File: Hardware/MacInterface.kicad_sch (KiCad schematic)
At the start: 11 parts, among them J1 650946-5, U2 SN74LVCH16T245, U3 SN74LVCH16T245, U4 SN74LVCH16T245, U5 68000-CPU, U6 68000-BOARD

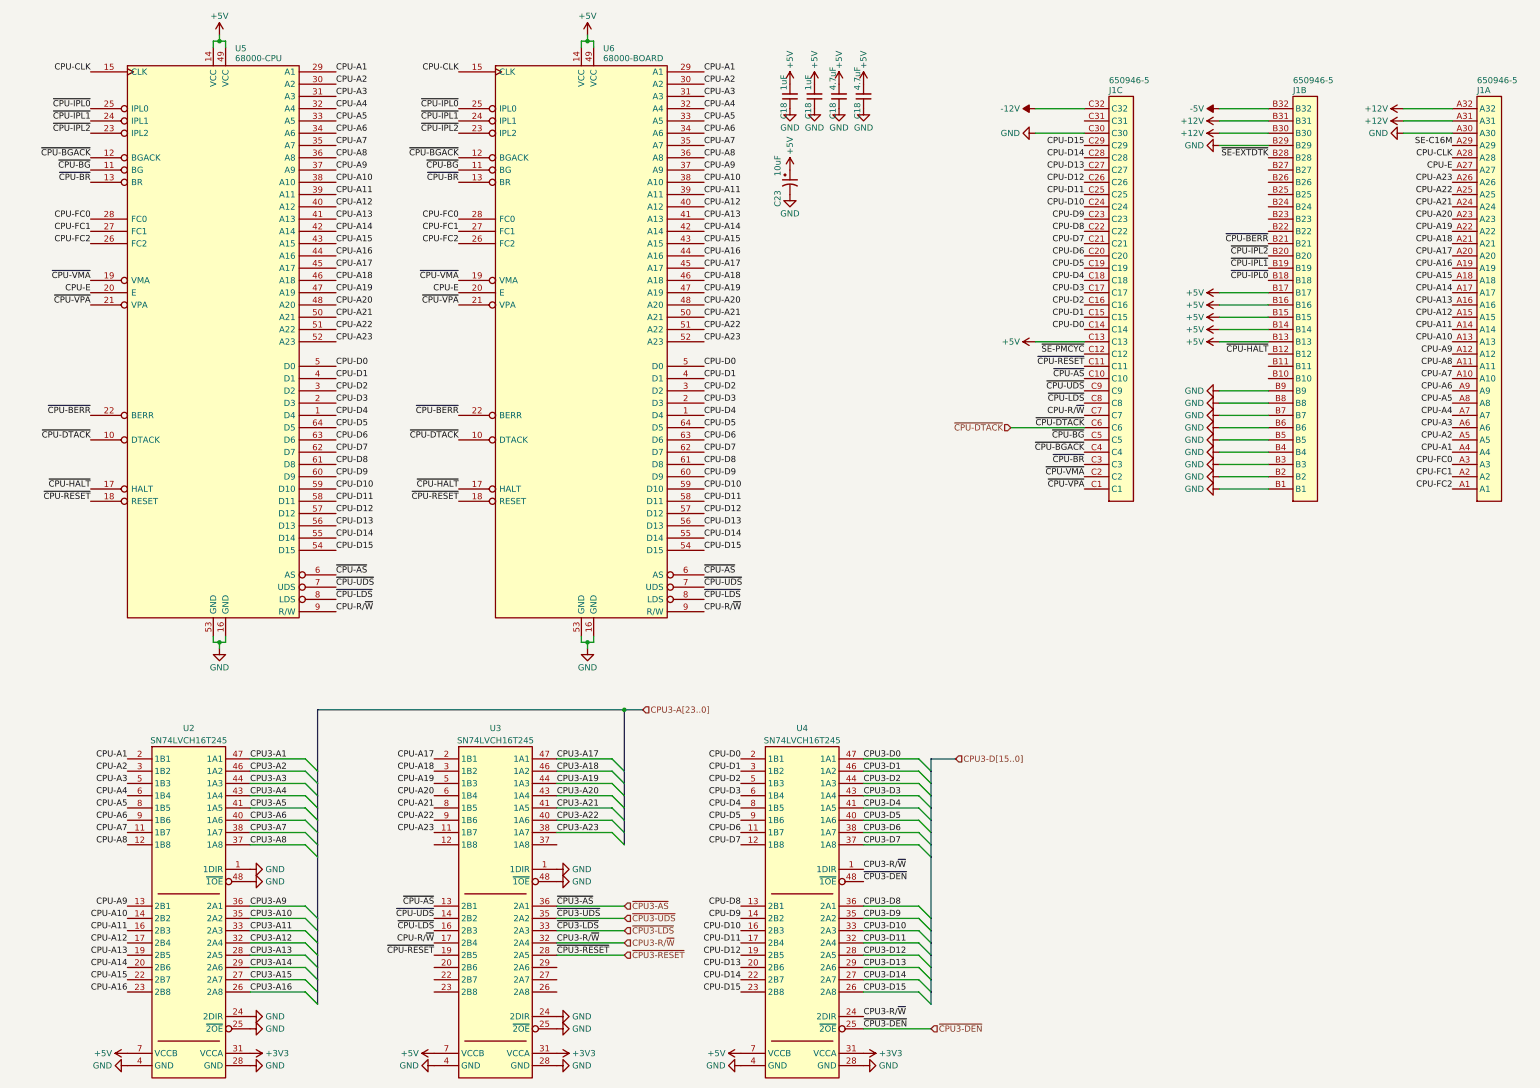
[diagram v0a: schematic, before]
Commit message: R3 Initial schematic complete, start routing
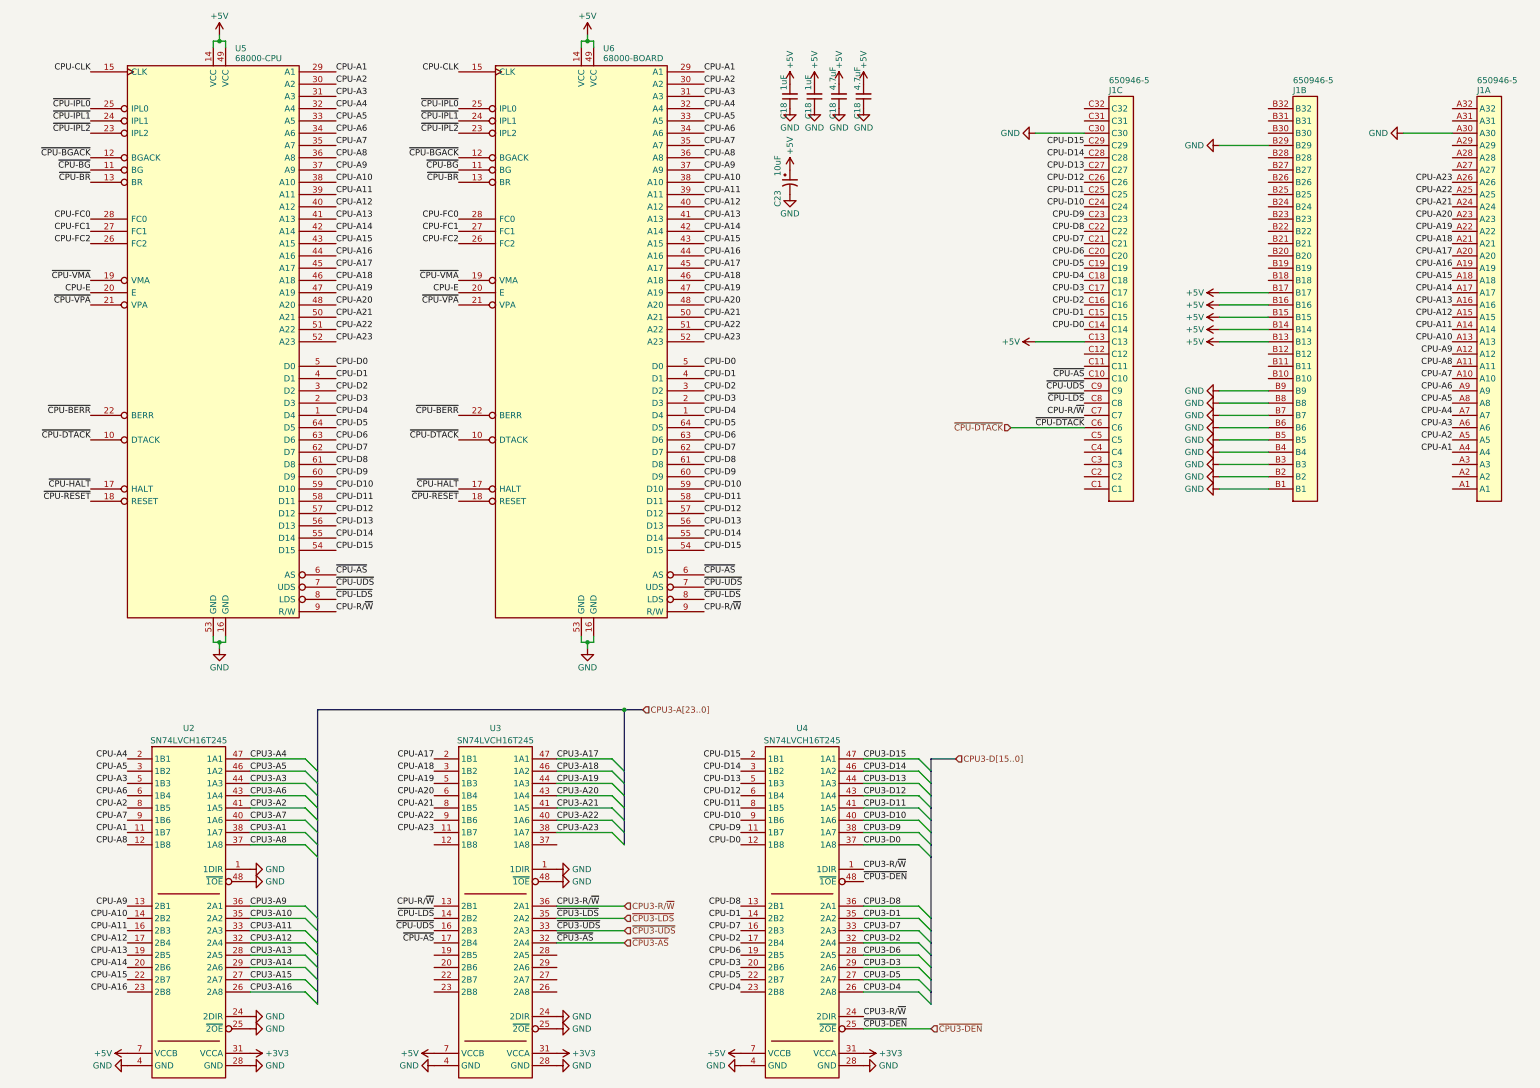
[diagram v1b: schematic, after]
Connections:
- net ~{CPU3-RESET} is gone; now on net GND: U3.28 (GND)
- net CPU-A1: now also U2.11 (1B7); no longer U2.2 (1B1)
- net CPU-A2: now also U2.8 (1B5); no longer U2.3 (1B2)
- net CPU-A4: now also U2.2 (1B1); no longer U2.6 (1B4)
- net CPU-A5: now also U2.3 (1B2); no longer U2.8 (1B5)
- net CPU-A6: now also U2.6 (1B4); no longer U2.9 (1B6)
- net CPU-A7: now also U2.9 (1B6); no longer U2.11 (1B7)
- net CPU-CLK: no longer J1.A28
- net CPU-D0: now also U4.12 (1B8); no longer U4.2 (1B1)
- net CPU-D1: now also U4.14 (2B2); no longer U4.3 (1B2)
- net CPU-D10: now also U4.9 (1B6); no longer U4.16 (2B3)
- net CPU-D11: now also U4.8 (1B5); no longer U4.17 (2B4)
- net CPU-D12: now also U4.6 (1B4); no longer U4.19 (2B5)
- net CPU-D13: now also U4.5 (1B3); no longer U4.20 (2B6)
- net CPU-D14: now also U4.3 (1B2); no longer U4.22 (2B7)
- net CPU-D15: now also U4.2 (1B1); no longer U4.23 (2B8)
- net CPU-D2: now also U4.17 (2B4); no longer U4.5 (1B3)
- net CPU-D3: now also U4.20 (2B6); no longer U4.6 (1B4)
- net CPU-D4: now also U4.23 (2B8); no longer U4.8 (1B5)
- net CPU-D5: now also U4.22 (2B7); no longer U4.9 (1B6)
- net CPU-D6: now also U4.19 (2B5); no longer U4.11 (1B7)
- net CPU-D7: now also U4.16 (2B3); no longer U4.12 (1B8)
- net CPU-D9: now also U4.11 (1B7); no longer U4.14 (2B2)
- net CPU-E: no longer J1.A27
- net CPU-FC0: no longer J1.A3
- net CPU-FC1: no longer J1.A2
- net CPU-FC2: no longer J1.A1
- net CPU-R/~{W}: now also U3.13 (2B1); no longer U3.17 (2B4)
- net CPU3-A1: now also U2.38 (1A7); no longer U2.47 (1A1)
- net CPU3-A2: now also U2.41 (1A5); no longer U2.46 (1A2)
- net CPU3-A4: now also U2.47 (1A1); no longer U2.43 (1A4)
- net CPU3-A5: now also U2.46 (1A2); no longer U2.41 (1A5)
- net CPU3-A6: now also U2.43 (1A4); no longer U2.40 (1A6)
- net CPU3-A7: now also U2.40 (1A6); no longer U2.38 (1A7)
- net CPU3-D0: now also U4.37 (1A8); no longer U4.47 (1A1)
- net CPU3-D1: now also U4.35 (2A2); no longer U4.46 (1A2)
- net CPU3-D10: now also U4.40 (1A6); no longer U4.33 (2A3)
- net CPU3-D11: now also U4.41 (1A5); no longer U4.32 (2A4)
- net CPU3-D12: now also U4.43 (1A4); no longer U4.28 (GND)
- net CPU3-D13: now also U4.44 (1A3); no longer U4.29 (2A6)
- net CPU3-D14: now also U4.46 (1A2); no longer U4.27 (2A7)
- net CPU3-D15: now also U4.47 (1A1); no longer U4.26 (2A8)
- net CPU3-D2: now also U4.32 (2A4); no longer U4.44 (1A3)
- net CPU3-D3: now also U4.29 (2A6); no longer U4.43 (1A4)
- net CPU3-D4: now also U4.26 (2A8); no longer U4.41 (1A5)
- net CPU3-D5: now also U4.27 (2A7); no longer U4.40 (1A6)
- net CPU3-D6: now also U4.28 (GND); no longer U4.38 (1A7)
- net CPU3-D7: now also U4.33 (2A3); no longer U4.37 (1A8)
- net CPU3-D9: now also U4.38 (1A7); no longer U4.35 (2A2)
- net CPU3-R/~{W}: now also U3.36 (2A1); no longer U3.32 (2A4)
- net ~{CPU-AS}: now also U3.17 (2B4); no longer U3.13 (2B1)
- net ~{CPU-BERR}: no longer J1.B21
- net ~{CPU-BGACK}: no longer J1.C4
- net ~{CPU-BG}: no longer J1.C5
- net ~{CPU-BR}: no longer J1.C3
- net ~{CPU-HALT}: no longer J1.B12
- net ~{CPU-IPL0}: no longer J1.B18
- net ~{CPU-IPL1}: no longer J1.B19
- net ~{CPU-IPL2}: no longer J1.B20
- net ~{CPU-LDS}: now also U3.14 (2B2); no longer U3.16 (2B3)
- net ~{CPU-RESET}: no longer J1.C11, U3.19 (2B5)
- net ~{CPU-UDS}: now also U3.16 (2B3); no longer U3.14 (2B2)
- net ~{CPU-VMA}: no longer J1.C2
- net ~{CPU-VPA}: no longer J1.C1
- net ~{CPU3-AS}: now also U3.32 (2A4); no longer U3.36 (2A1)
- net ~{CPU3-LDS}: now also U3.35 (2A2); no longer U3.33 (2A3)
- net ~{CPU3-UDS}: now also U3.33 (2A3); no longer U3.35 (2A2)
- removed net +12V: J1.A31, J1.A32, J1.B30, J1.B31
- net -12V: no longer names the net of J1.C32
- net -5V: no longer names the net of J1.B32
- net SE-C16M: no longer names the net of J1.A29
- net ~{SE-EXTDTK}: no longer names the net of J1.B28
- net ~{SE-PMCYC}: no longer names the net of J1.C12

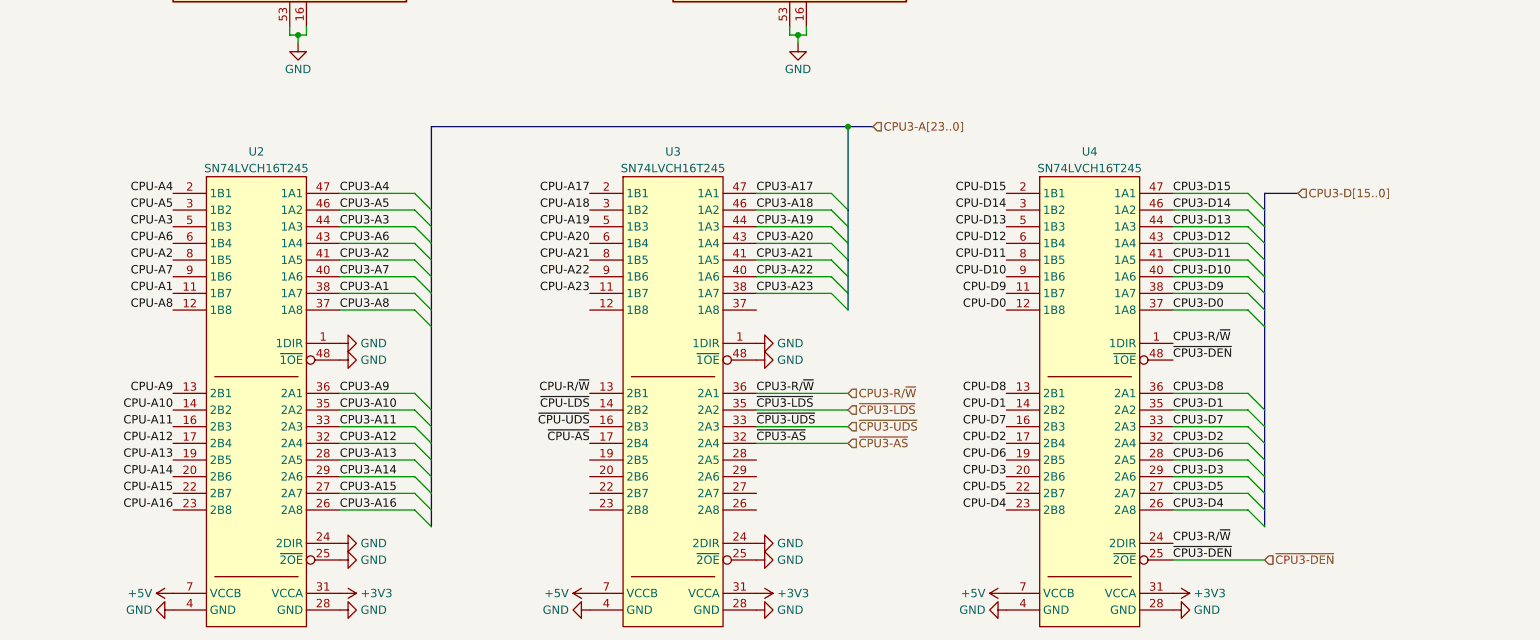
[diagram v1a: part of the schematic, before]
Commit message: Multiplex CPU bus and add 24bpp output
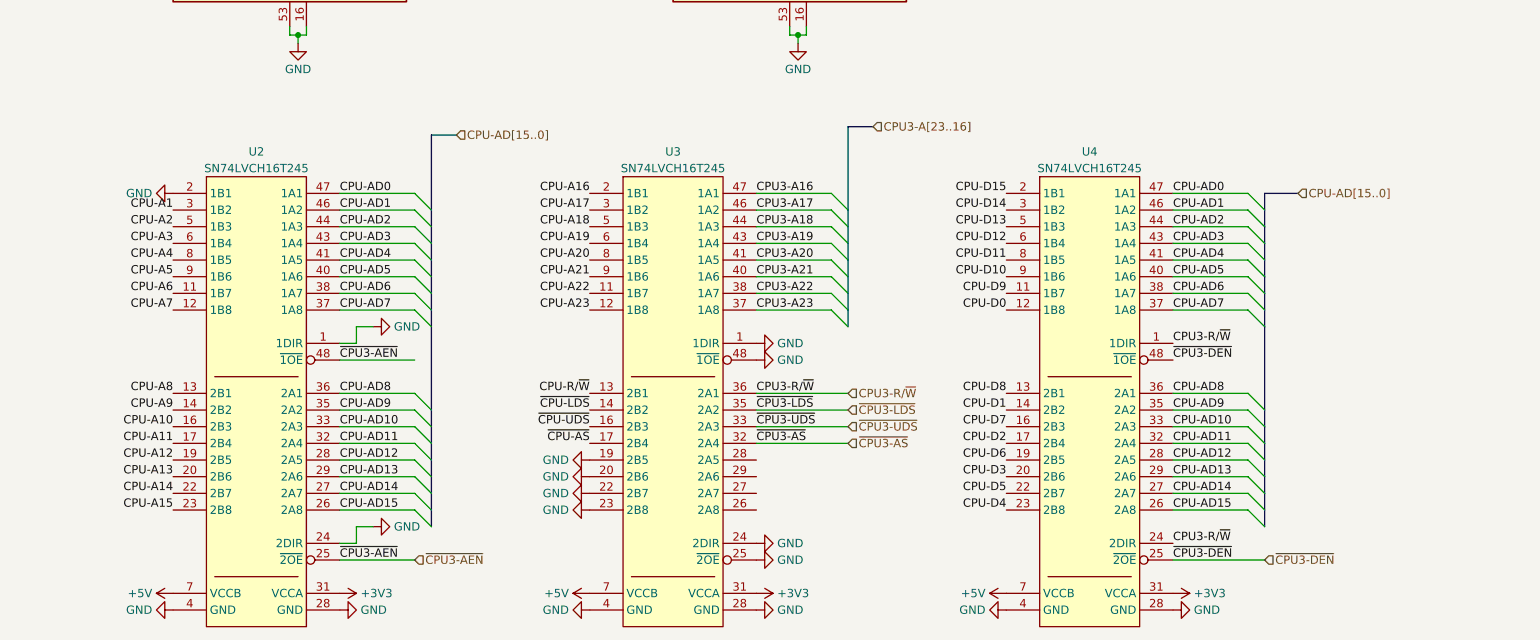
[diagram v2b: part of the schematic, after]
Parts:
- C18: footprint Capacitor_SMD:C_0805_2012Metric_Pad1.18x1.45mm_HandSolder -> Capacitor_SMD:C_0402_1005Metric
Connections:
- net CPU3-A13 is gone; now on net GND: U2.28 (GND)
- net CPU3-D0 is gone; now on net CPU-AD7: U4.37 (1A8)
- net CPU3-D1 is gone; now on net CPU-AD9: U4.35 (2A2)
- net CPU3-D10 is gone; now on net CPU-AD5: U4.40 (1A6)
- net CPU3-D11 is gone; now on net CPU-AD4: U4.41 (1A5)
- net CPU3-D12 is gone; now on net CPU-AD3: U4.43 (1A4)
- net CPU3-D13 is gone; now on net CPU-AD2: U4.44 (1A3)
- net CPU3-D14 is gone; now on net CPU-AD1: U4.46 (1A2)
- net CPU3-D15 is gone; now on net CPU-AD0: U4.47 (1A1)
- net CPU3-D2 is gone; now on net CPU-AD11: U4.32 (2A4)
- net CPU3-D3 is gone; now on net CPU-AD13: U4.29 (2A6)
- net CPU3-D5 is gone; now on net CPU-AD14: U4.27 (2A7)
- net CPU3-D6 is gone; now on net GND: U4.28 (GND)
- net CPU3-D7 is gone; now on net CPU-AD10: U4.33 (2A3)
- net CPU3-D8 is gone; now on net CPU-AD8: U4.36 (2A1)
- net CPU3-D9 is gone; now on net CPU-AD6: U4.38 (1A7)
- net CPU-A1: now also U2.3 (1B2); no longer U2.11 (1B7)
- net CPU-A10: now also U2.16 (2B3); no longer U2.14 (2B2)
- net CPU-A11: now also U2.17 (2B4); no longer U2.16 (2B3)
- net CPU-A12: now also U2.19 (2B5); no longer U2.17 (2B4)
- net CPU-A13: now also U2.20 (2B6); no longer U2.19 (2B5)
- net CPU-A14: now also U2.22 (2B7); no longer U2.20 (2B6)
- net CPU-A15: now also U2.23 (2B8); no longer U2.22 (2B7)
- net CPU-A16: now also U3.2 (1B1); no longer U2.23 (2B8)
- net CPU-A17: now also U3.3 (1B2); no longer U3.2 (1B1)
- net CPU-A18: now also U3.5 (1B3); no longer U3.3 (1B2)
- net CPU-A19: now also U3.6 (1B4); no longer U3.5 (1B3)
- net CPU-A2: now also U2.5 (1B3); no longer U2.8 (1B5)
- net CPU-A20: now also U3.8 (1B5); no longer U3.6 (1B4)
- net CPU-A21: now also U3.9 (1B6); no longer U3.8 (1B5)
- net CPU-A22: now also U3.11 (1B7); no longer U3.9 (1B6)
- net CPU-A23: now also U3.12 (1B8); no longer U3.11 (1B7)
- net CPU-A3: now also U2.6 (1B4); no longer U2.5 (1B3)
- net CPU-A4: now also U2.8 (1B5); no longer U2.2 (1B1)
- net CPU-A5: now also U2.9 (1B6); no longer U2.3 (1B2)
- net CPU-A6: now also U2.11 (1B7); no longer U2.6 (1B4)
- net CPU-A7: now also U2.12 (1B8); no longer U2.9 (1B6)
- net CPU-A8: now also U2.13 (2B1); no longer U2.12 (1B8)
- net CPU-A9: now also U2.14 (2B2); no longer U2.13 (2B1)
- net CPU3-A16: now also U3.47 (1A1); no longer U2.26 (2A8)
- net CPU3-A17: now also U3.46 (1A2); no longer U3.47 (1A1)
- net CPU3-A18: now also U3.44 (1A3); no longer U3.46 (1A2)
- net CPU3-A19: now also U3.43 (1A4); no longer U3.44 (1A3)
- net CPU3-A20: now also U3.41 (1A5); no longer U3.43 (1A4)
- net CPU3-A21: now also U3.40 (1A6); no longer U3.41 (1A5)
- net CPU3-A22: now also U3.38 (1A7); no longer U3.40 (1A6)
- net CPU3-A23: now also U3.37 (1A8); no longer U3.38 (1A7)
- net GND: now also U2.2 (1B1), U3.19 (2B5), U3.20 (2B6), U3.22 (2B7), U3.23 (2B8); no longer U2.25 (~{2OE}), U2.48 (~{1OE})
- net CPU3-A1 renamed CPU-AD6
- net CPU3-A10 renamed CPU-AD9
- net CPU3-A11 renamed CPU-AD10
- net CPU3-A12 renamed CPU-AD11
- net CPU3-A14 renamed CPU-AD13
- net CPU3-A15 renamed CPU-AD14
- net CPU3-A2 renamed CPU-AD4
- net CPU3-A3 renamed CPU-AD2
- net CPU3-A4 renamed CPU-AD0
- net CPU3-A5 renamed CPU-AD1
- net CPU3-A6 renamed CPU-AD3
- net CPU3-A7 renamed CPU-AD5
- net CPU3-A8 renamed CPU-AD7
- net CPU3-A9 renamed CPU-AD8
- net CPU3-D4 renamed CPU-AD15
- net CPU-AD15: now also U2.26 (2A8)
- new net CPU-AD12: U2.28 (GND), U4.28 (GND)
- new net ~{CPU3-AEN}: U2.25 (~{2OE}), U2.48 (~{1OE})
